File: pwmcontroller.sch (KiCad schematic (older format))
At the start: 13 parts, among them J1 CONN_01X04, J2 CONN_01X04, U1 WPMIx9200501S, U2 NE555

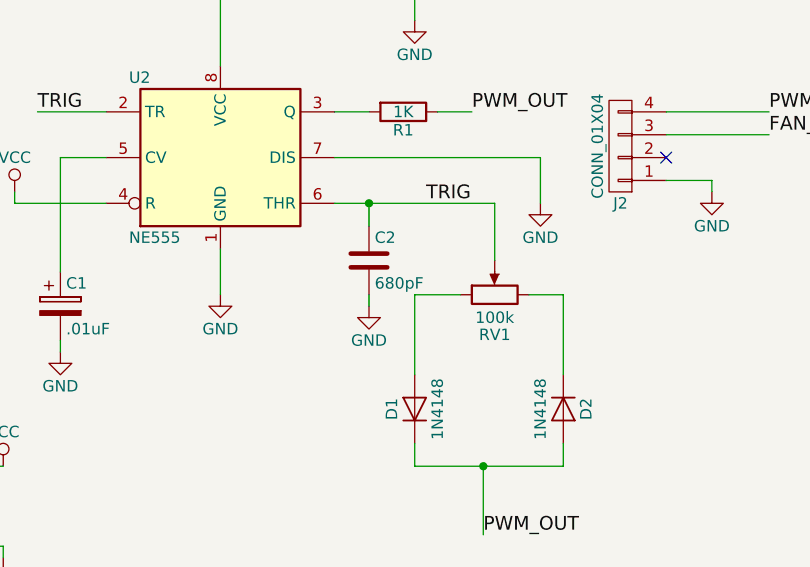
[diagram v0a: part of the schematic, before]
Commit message: Change C2 to 470pF
After doing some breadboard testing the carrier frequency of the PWM
signal was too low at only ~12kHz to ~14kHz. The PWM fan spec says this
needs to be nominally 25kHz with a range of 21kHz to 28kHz. By
decreasing the capacitance of the C2 to 470pF from 680pF this should
adjust the frequency to be in this range. Next time I'll do the
arithmetic before ordering parts.
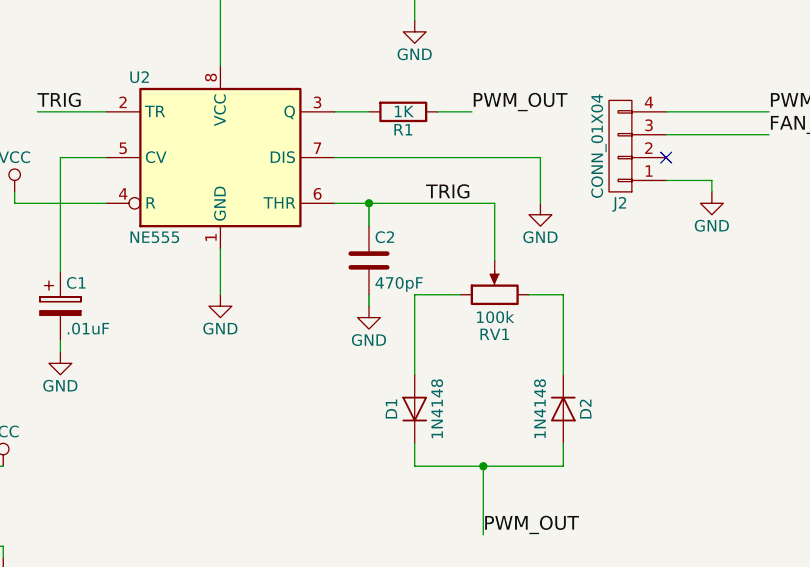
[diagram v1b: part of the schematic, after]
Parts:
- C2: value 680pF -> 470pF
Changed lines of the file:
@@
 P 4500 4150
 F 0 "C2" H 4525 4250 50  0000 L CNN
-F 1 "680pF" H 4525 4050 50  0000 L CNN
+F 1 "470pF" H 4525 4050 50  0000 L CNN
 F 2 "Capacitors_THT:C_Disc_D4.7mm_W2.5mm_P5.00mm" H 4538 4000 50  0001 C CNN
 F 3 "" H 4500 4150 50  0001 C CNN

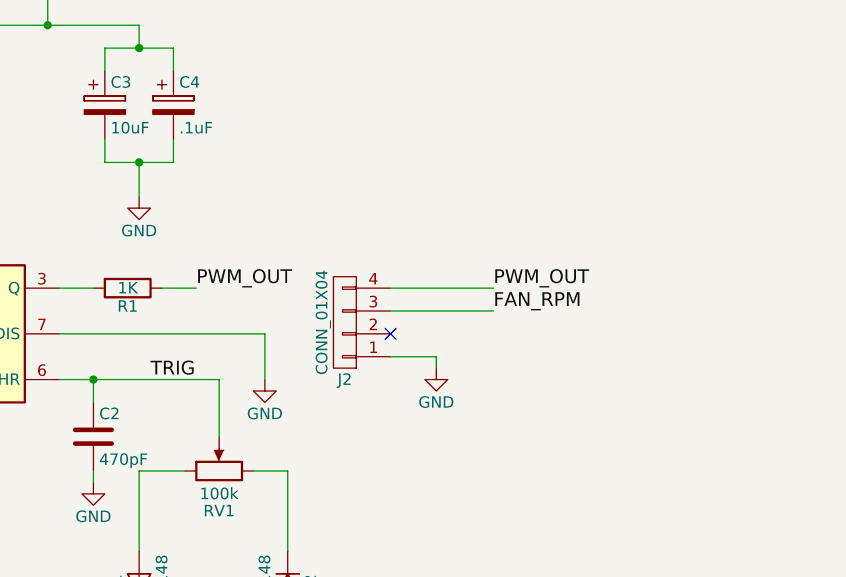
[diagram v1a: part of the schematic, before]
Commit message: Add Schmitt Trigger Output Buffer
This commit adds a schmitt trigger output buffer to clean up the output
signal.
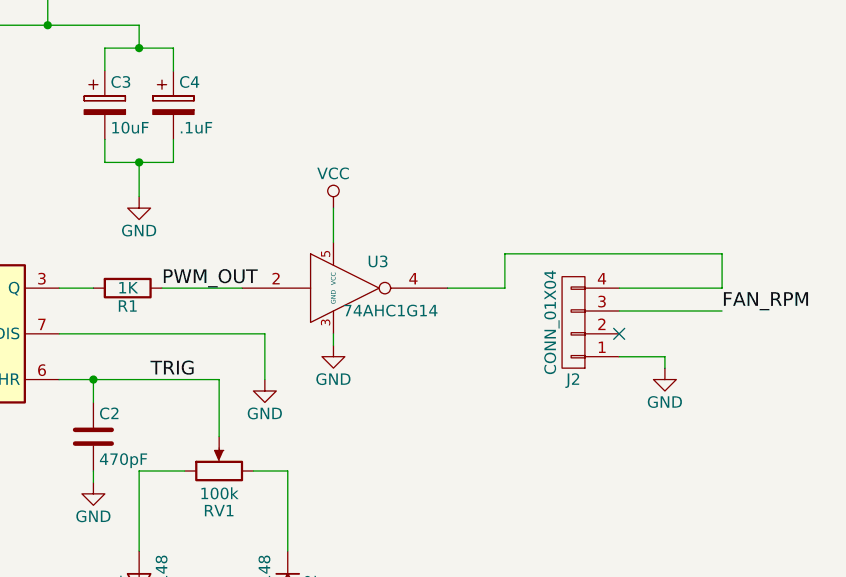
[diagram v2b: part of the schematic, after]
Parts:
- added U3: 74AHC1G14, TO_SOT_Packages_SMD:SOT-23-5_HandSoldering, symbol 74AHC1G14
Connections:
- net GND: now also U3.3 (GND)
- net PWM_OUT: now also U3.2; no longer J2.4 (P4)
- net VCC: now also U3.5 (VCC)
- new net: J2.4 (P4), U3.4
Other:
- moved on the sheet: J2
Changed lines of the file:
@@
 L CONN_01X04 J2
 U 1 1 59B30621
-P 5600 3650
-F 0 "J2" H 5600 3900 50  0000 C CNN
-F 1 "CONN_01X04" V 5700 3650 50  0000 C CNN
-F 2 "Connectors_Molex:Molex_KK-6410-04_04x2.54mm_Straight" H 5600 3650 50  0001 C CNN
-F 3 "" H 5600 3650 50  0001 C CNN
-	1    5600 3650
+P 6600 3650
+F 0 "J2" H 6600 3900 50  0000 C CNN
+F 1 "CONN_01X04" V 6700 3650 50  0000 C CNN
+F 2 "Connectors_Molex:Molex_KK-6410-04_04x2.54mm_Straight" H 6600 3650 50  0001 C CNN
+F 3 "" H 6600 3650 50  0001 C CNN
+	1    6600 3650
 	-1   0    0    1
 $EndComp
@@
 L GND #PWR15
 U 1 1 59C04D5D
-P 6000 3850
-F 0 "#PWR15" H 6000 3600 50  0001 C CNN
-F 1 "GND" H 6000 3700 50  0000 C CNN
-F 2 "" H 6000 3850 50  0001 C CNN
-F 3 "" H 6000 3850 50  0001 C CNN
-	1    6000 3850
+P 7000 3850
+F 0 "#PWR15" H 7000 3600 50  0001 C CNN
+F 1 "GND" H 7000 3700 50  0000 C CNN
+F 2 "" H 7000 3850 50  0001 C CNN
+F 3 "" H 7000 3850 50  0001 C CNN
+	1    7000 3850
 	1    0    0    -1
 $EndComp
@@
 	1400 3500 1400 3900
 Wire Wire Line
-	5800 3800 6000 3800
-Wire Wire Line
-	6000 3800 6000 3850
+	6800 3800 7000 3800
+Wire Wire Line
+	7000 3800 7000 3850
 Wire Wire Line
 	2050 3700 1600 3700
 Wire Wire Line
-	5800 3600 6250 3600
-Text Label 6250 3600 0    60   ~ 0
+	6800 3600 7250 3600
+Text Label 7250 3600 0    60   ~ 0
 FAN_RPM
 Text Label 1600 3700 0    60   ~ 0
@@
 $EndComp
 Wire Wire Line
-	5800 3500 6250 3500
-Text Label 6250 3500 0    60   ~ 0
-PWM_OUT
+	6800 3500 7250 3500
 $Comp
 L GND #PWR10
@@
 Wire Wire Line
 	4350 3500 4500 3500
-Text Label 4950 3500 0    60   ~ 0
+Text Label 4800 3500 0    60   ~ 0
 PWM_OUT
 Wire Wire Line
-	4800 3500 4950 3500
+	4800 3500 5150 3500
 $Comp
 L CP C1
@@
 	1    0    0    -1
 $EndComp
-NoConn ~ 5800 3700
+NoConn ~ 6800 3700
+$Comp
+L 74AHC1G14 U3
+U 1 1 59E829E5
+P 5600 3500
+F 0 "U3" H 5745 3615 50  0000 C CNN
+F 1 "74AHC1G14" H 5800 3400 50  0000 C CNN
+F 2 "TO_SOT_Packages_SMD:SOT-23-5_HandSoldering" H 5695 3365 50  0001 C CNN
+F 3 "" H 5745 3615 50  0001 C CNN
+	1    5600 3500
+	1    0    0    -1
+$EndComp
+$Comp
+L GND #PWR?
+U 1 1 59E82C69
+P 5550 3750
+F 0 "#PWR?" H 5550 3500 50  0001 C CNN
+F 1 "GND" H 5550 3600 50  0000 C CNN
+F 2 "" H 5550 3750 50  0001 C CNN
+F 3 "" H 5550 3750 50  0001 C CNN
+	1    5550 3750
+	1    0    0    -1
+$EndComp
+Wire Wire Line
+	5550 3700 5550 3750
+$Comp
+L VCC #PWR?
+U 1 1 59E82CF7
+P 5550 3150
+F 0 "#PWR?" H 5550 3000 50  0001 C CNN
+F 1 "VCC" H 5550 3300 50  0000 C CNN
+F 2 "" H 5550 3150 50  0001 C CNN
+F 3 "" H 5550 3150 50  0001 C CNN
+	1    5550 3150
+	1    0    0    -1
+$EndComp
+Wire Wire Line
+	5550 3150 5550 3300
+Wire Wire Line
+	6050 3500 6300 3500
+Wire Wire Line
+	7250 3500 7250 3350
+Wire Wire Line
+	7250 3350 6300 3350
+Wire Wire Line
+	6300 3350 6300 3500
 $EndSCHEMATC

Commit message: Fix floating output ground
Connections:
- net GNDS is gone; now on net GND: J1.1 (P1), U1.1 (-VIN)
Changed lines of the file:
@@
 	3150 4500 3150 4550
-$Comp
-L GNDS #PWR3
-U 1 1 59C0591F
-P 1400 3900
-F 0 "#PWR3" H 1400 3650 50  0001 C CNN
-F 1 "GNDS" H 1400 3750 50  0000 C CNN
-F 2 "" H 1400 3900 50  0001 C CNN
-F 3 "" H 1400 3900 50  0001 C CNN
-	1    1400 3900
-	1    0    0    -1
-$EndComp
 $Comp
 L WPMIx9200501S U1
@@
 F 3 "" H 2050 5300 60  0001 C CNN
 	1    2050 5300
-	1    0    0    -1
-$EndComp
-$Comp
-L GNDS #PWR2
-U 1 1 59C0605E
-P 1250 5100
-F 0 "#PWR2" H 1250 4850 50  0001 C CNN
-F 1 "GNDS" H 1250 4950 50  0000 C CNN
-F 2 "" H 1250 5100 50  0001 C CNN
-F 3 "" H 1250 5100 50  0001 C CNN
-	1    1250 5100
 	1    0    0    -1
 $EndComp
@@
 Wire Wire Line
 	6300 3350 6300 3500
+$Comp
+L GND #PWR?
+U 1 1 5A54137B
+P 1250 5100
+F 0 "#PWR?" H 1250 4850 50  0001 C CNN
+F 1 "GND" H 1250 4950 50  0000 C CNN
+F 2 "" H 1250 5100 50  0001 C CNN
+F 3 "" H 1250 5100 50  0001 C CNN
+	1    1250 5100
+	1    0    0    -1
+$EndComp
+$Comp
+L GND #PWR?
+U 1 1 5A541605
+P 1400 3900
+F 0 "#PWR?" H 1400 3650 50  0001 C CNN
+F 1 "GND" H 1400 3750 50  0000 C CNN
+F 2 "" H 1400 3900 50  0001 C CNN
+F 3 "" H 1400 3900 50  0001 C CNN
+	1    1400 3900
+	1    0    0    -1
+$EndComp
 $EndSCHEMATC

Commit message: Pivot to revision 3 of the design
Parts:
- removed U1: WPMIx9200501S, pwmcontroller:WPMIx9200501S, symbol WPMIx9200501S
- added C5: .33uF, Capacitors_THT:CP_Radial_D5.0mm_P2.00mm, symbol pwmcontroller-rescue:CP
- added C6: .1uF, Capacitors_THT:C_Disc_D4.7mm_W2.5mm_P5.00mm, symbol pwmcontroller-rescue:CP
- added J3: Conn_01x02_Male, Socket_Strips:Socket_Strip_Straight_1x02_Pitch2.54mm, symbol Connector:Conn_01x02_Male
- added U1: MC78L05_TO92, TO_SOT_Packages_THT:TO-92_Molded_Narrow, symbol Regulator_Linear:MC78L05_TO92
- C1, C3, C4: symbol CP -> pwmcontroller-rescue:CP
- C2: symbol C -> pwmcontroller-rescue:C
- D1, D2: symbol D -> pwmcontroller-rescue:D
- J1, J2: symbol CONN_01X04 -> pwmcontroller-rescue:CONN_01X04
- R1, R2: symbol R -> pwmcontroller-rescue:R
- RV1: symbol POT -> pwmcontroller-rescue:POT
- U2: symbol NE555 -> pwmcontroller-rescue:NE555
- U3: symbol 74AHC1G14 -> pwmcontroller-rescue:74AHC1G14
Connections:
- net +12V: now also C5.1, J3.1 (Pin_1), U1.3 (VI)
- net GND: now also C5.2, C6.2, U1.2 (GND)
- net VCC: now also C6.1, U1.1 (VO)
- net 12V_OUT: now reaches J2.2 (P2)
- net 12V_OUT: now also J3.2 (Pin_2)
- no-connect marks 1 -> 0
